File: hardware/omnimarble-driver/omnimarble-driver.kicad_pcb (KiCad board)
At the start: 4 copper layers, 220 x 150 mm, 178 parts, among them J1 BarrelJack_Horizontal, J10 PinSocket_1x20_P2.54mm_Vertic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, J11 PinHeader_2x13_P2.54mm_Vertic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, J2 TerminalBarrier_1x02_P9.50mm, J3 PinHeader_1x02_P2.54mm_Vertic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, J4 PinHeader_1x03_P2.54mm_Vertic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, J5 TerminalBarrier_1x02_P9.50mm, J6 IDC-Header_2x05_P2.54mm_Verti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, J7 IDC-Header_2x05_P2.54mm_Verti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, J8 JST_XH_B4B-XH-A_1x04_P2.50mm_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, J9 PinSocket_1x20_P2.54mm_Vertic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, K1 Relay_HF3FF_T73, K2 Relay_HF3FF_T73, Q1 SOT-23, Q10 TOLL-8, Q11 TOLL-8, Q12 TOLL-8, Q2 SOT-23, Q3 SOT-23, Q4 SOT-23, Q90 TO-252-2, Q91 TO-252-2, U1 TSOT-23-6, U10 VSSOP-8_2.3x2mm_P0.5mm, U11 SOIC-14_3.9x8.7mm_P1.27mm, U12 SOIC-14_3.9x8.7mm_P1.27mm, U2 SOT-89-3, U3 SOIC-8_3.9x4.9mm_P1.27mm, U4 SOIC-8_3.9x4.9mm_P1.27mm, U5 SOT-23, U6 SOT-353_SC-70-5, U7 SOIC-8_3.9x4.9mm_P1.27mm, U8 SOIC-8_3.9x4.9mm_P1.27mm, U9 TSSOP-8_3x3mm_P0.65mm

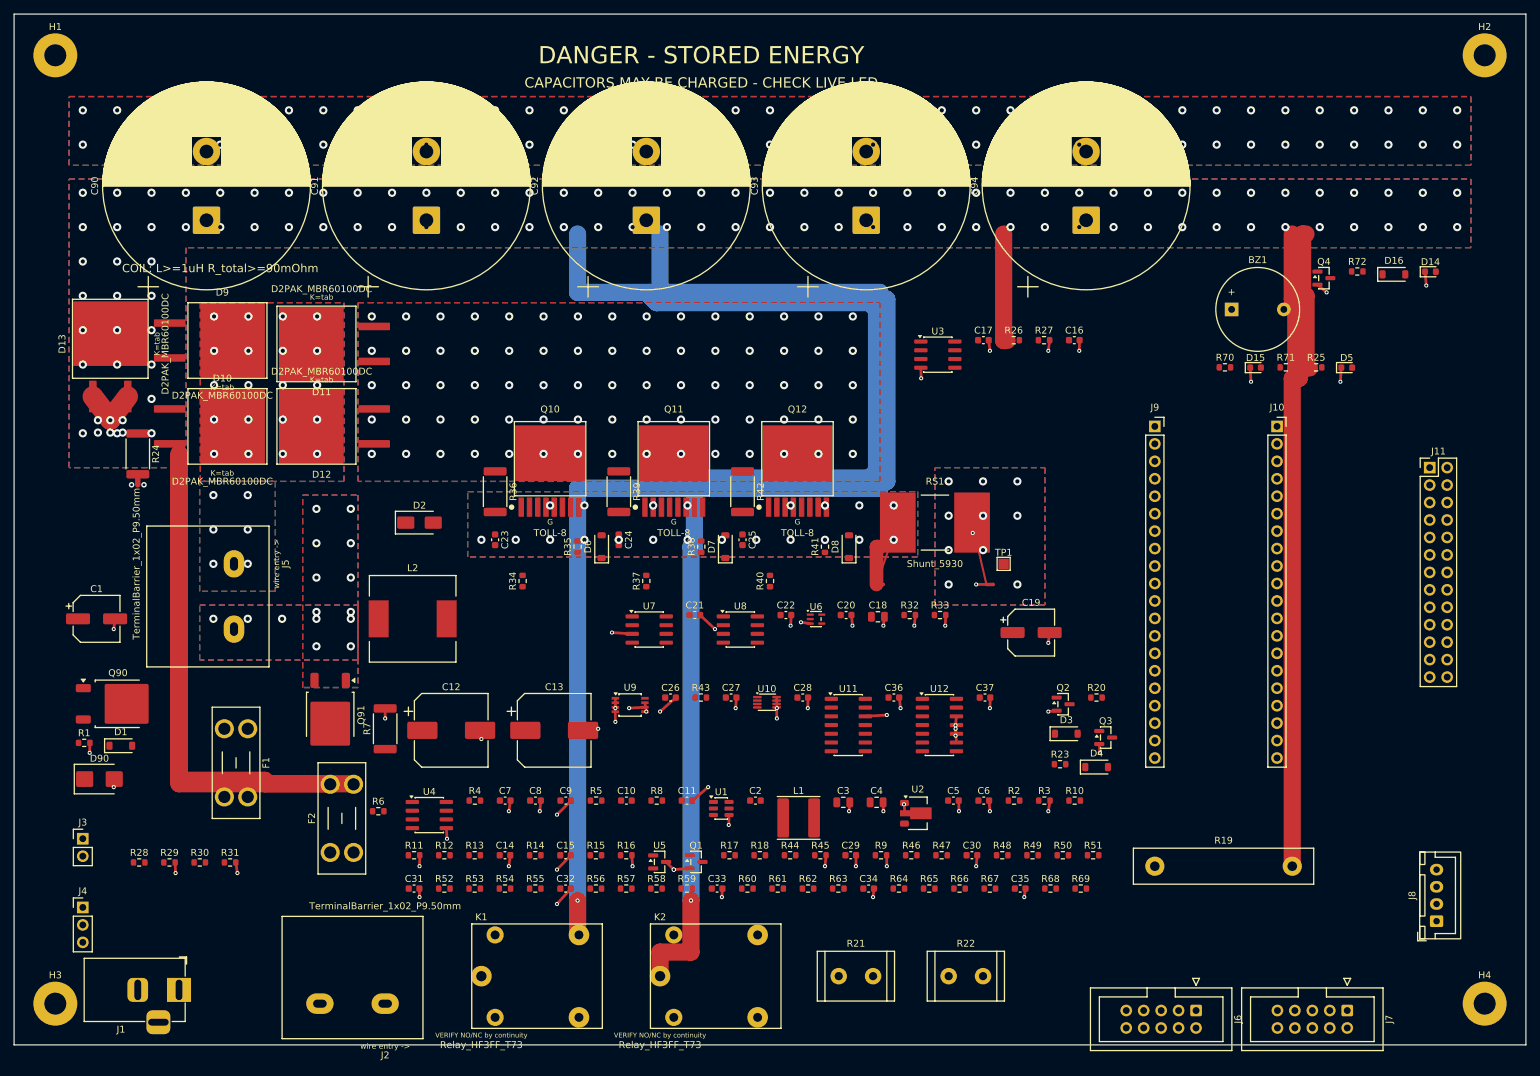
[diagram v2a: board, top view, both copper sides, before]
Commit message: Driver PCB: zero-shorts routing via parallel PathFinder negotiation
- gen_pcb.py: multiprocessing negotiation (24 workers, shared-memory
  usage/hist, sub-batch dispatch, ~14x wall time), best-state snapshot
  with restore-before-emit, stagnation break, width-aware swaths in all
  A* passes, verify-before-emit, contested-cell sentinel, tie/stub body
  checks, GND-drop relaxed site tests + far-ring recovery, straggler
  width ladder, geometric purge_track_shorts backstop
- route_worker.py: pcbnew-free worker module (Windows spawn safe)
- Board DRC: shorting_items 199 -> 0, tracks_crossing 25 -> 0,
  clearance 499 -> 56; unconnected 143 (honest residue: 52 route
  failures + GND drops + purged stubs) for the repair phase
- Reproducibility: deterministic across runs, worktree result
  reproduced exactly on main tree

Co-Authored-By: Claude Fable 5 <noreply@anthropic.com>
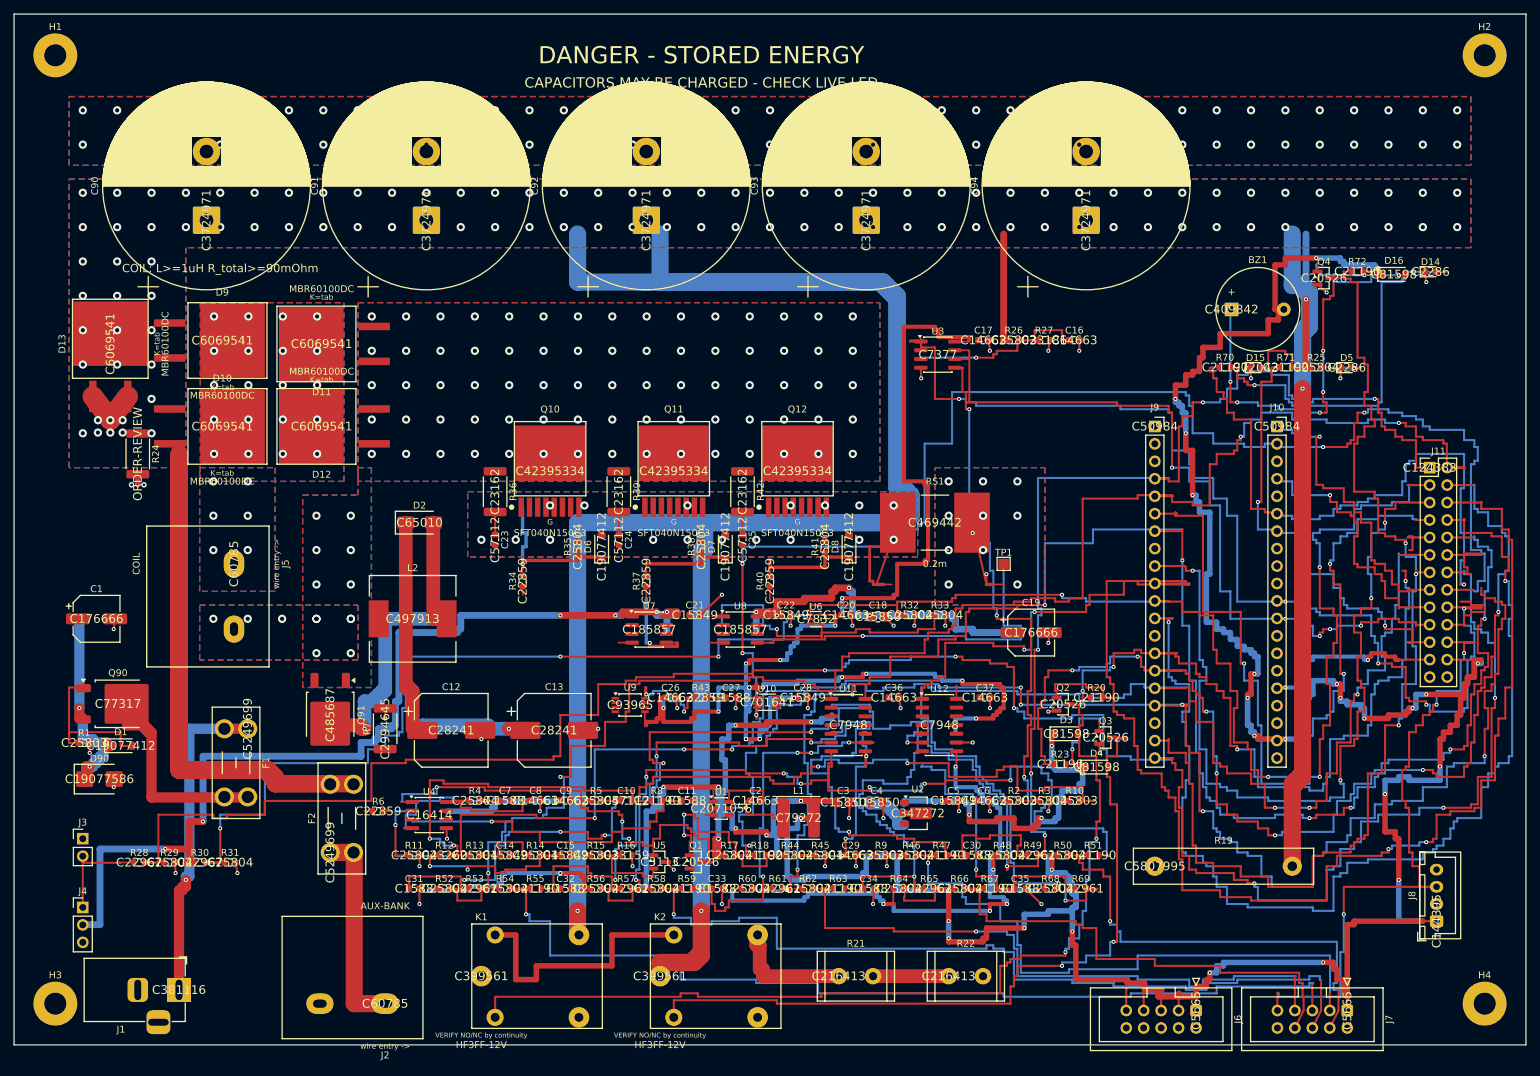
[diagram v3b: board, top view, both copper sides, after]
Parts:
- BZ1: value Buzzer_12x9.5RM7.6 -> buzzer-5V; footprint Buzzer_12x9.5RM7.6 -> Buzzer_Beeper:Buzzer_12x9.5RM7.6
- C1, C19: value CP_Elec_6.3x7.7 -> 100u-35V; footprint CP_Elec_6.3x7.7 -> Capacitor_SMD:CP_Elec_6.3x7.7
- C10, C23, C24, C25: value C_0603_1608Metric -> 10n; footprint C_0603_1608Metric -> Capacitor_SMD:C_0603_1608Metric
- C11, C27, C30, C31, C32, C33, C34, C35, C7: value C_0603_1608Metric -> 1n; footprint C_0603_1608Metric -> Capacitor_SMD:C_0603_1608Metric
- C12, C13: value CP_Elec_10x10.5 -> 100u-63V; footprint CP_Elec_10x10.5 -> Capacitor_SMD:CP_Elec_10x10.5
- C14, C15, C21, C22, C28, C5: value C_0603_1608Metric -> 1u; footprint C_0603_1608Metric -> Capacitor_SMD:C_0603_1608Metric
- C16, C17, C2, C20, C26, C29, C36, C37, C6, C8, C9: value C_0603_1608Metric -> 100n; footprint C_0603_1608Metric -> Capacitor_SMD:C_0603_1608Metric
- C18, C3, C4: value C_0805_2012Metric -> 10u; footprint C_0805_2012Metric -> Capacitor_SMD:C_0805_2012Metric
- C90, C91, C92, C93, C94: value CP_Radial_D30.0mm_P10.00mm_SnapIn -> 2200u-63V; footprint CP_Radial_D30.0mm_P10.00mm_SnapIn -> Capacitor_THT:CP_Radial_D30.0mm_P10.00mm_SnapIn
- D1, D6, D7, D8: value D_SOD-123 -> BZT52C15; footprint D_SOD-123 -> Diode_SMD:D_SOD-123
- D10, D11, D12, D13, D9: value D2PAK_MBR60100DC -> MBR60100DC; footprint D2PAK_MBR60100DC -> omnimarble:D2PAK_MBR60100DC
- D14, D5: value LED_0603_1608Metric -> LED_red; footprint LED_0603_1608Metric -> LED_SMD:LED_0603_1608Metric
- D15: value LED_0603_1608Metric -> LED_green; footprint LED_0603_1608Metric -> LED_SMD:LED_0603_1608Metric
- D16, D3, D4: value D_SOD-123 -> 1N4148W; footprint D_SOD-123 -> Diode_SMD:D_SOD-123
- D2: value D_SMA -> SS510; footprint D_SMA -> Diode_SMD:D_SMA
- D90: value D_SMB -> SMBJ33A; footprint D_SMB -> Diode_SMD:D_SMB
- F1: value Fuseholder_Blade_Mini_Keystone_3568 -> 5A-MINI; footprint Fuseholder_Blade_Mini_Keystone_3568 -> Fuse:Fuseholder_Blade_Mini_Keystone_3568
- F2: value Fuseholder_Blade_Mini_Keystone_3568 -> 30A-MINI; footprint Fuseholder_Blade_Mini_Keystone_3568 -> Fuse:Fuseholder_Blade_Mini_Keystone_3568
- J1: value BarrelJack_Horizontal -> 24V-IN; footprint BarrelJack_Horizontal -> Connector_BarrelJack:BarrelJack_Horizontal
- J10, J9: value PinSocket_1x20_P2.54mm_Vertical -> PICO-SOCKET; footprint PinSocket_1x20_P2.54mm_Vertical -> Connector_PinSocket_2.54mm:PinSocket_1x20_P2.54mm_Vertical
- J11: value PinHeader_2x13_P2.54mm_Vertical -> IO-BREAKOUT; footprint PinHeader_2x13_P2.54mm_Vertical -> Connector_PinHeader_2.54mm:PinHeader_2x13_P2.54mm_Vertical
- J2: value TerminalBarrier_1x02_P9.50mm -> AUX-BANK; footprint TerminalBarrier_1x02_P9.50mm -> omnimarble:TerminalBarrier_1x02_P9.50mm
- J3: value PinHeader_1x02_P2.54mm_Vertical -> E-STOP-NC; footprint PinHeader_1x02_P2.54mm_Vertical -> Connector_PinHeader_2.54mm:PinHeader_1x02_P2.54mm_Vertical
- J4: value PinHeader_1x03_P2.54mm_Vertical -> ARM-KEY; footprint PinHeader_1x03_P2.54mm_Vertical -> Connector_PinHeader_2.54mm:PinHeader_1x03_P2.54mm_Vertical
- J5: value TerminalBarrier_1x02_P9.50mm -> COIL; footprint TerminalBarrier_1x02_P9.50mm -> omnimarble:TerminalBarrier_1x02_P9.50mm
- J6: value IDC-Header_2x05_P2.54mm_Vertical -> RAIL-EMIT; footprint IDC-Header_2x05_P2.54mm_Vertical -> Connector_IDC:IDC-Header_2x05_P2.54mm_Vertical
- J7: value IDC-Header_2x05_P2.54mm_Vertical -> RAIL-RECV; footprint IDC-Header_2x05_P2.54mm_Vertical -> Connector_IDC:IDC-Header_2x05_P2.54mm_Vertical
- J8: value JST_XH_B4B-XH-A_1x04_P2.50mm_Vertical -> SPARE-JST; footprint JST_XH_B4B-XH-A_1x04_P2.50mm_Vertical -> Connector_JST:JST_XH_B4B-XH-A_1x04_P2.50mm_Vertical
- K1, K2: value Relay_HF3FF_T73 -> HF3FF-12V; footprint Relay_HF3FF_T73 -> omnimarble:Relay_HF3FF_T73
- L1: value L_Changjiang_FNR6045S -> 10uH; footprint L_Changjiang_FNR6045S -> Inductor_SMD:L_Changjiang_FNR6045S
- L2: value L_12x12mm_H8mm -> 47uH; footprint L_12x12mm_H8mm -> Inductor_SMD:L_12x12mm_H8mm
- NT1, NT2: value NetTie-2_SMD_Pad0.5mm -> NetTie; footprint NetTie-2_SMD_Pad0.5mm -> NetTie:NetTie-2_SMD_Pad0.5mm
- Q1, Q2, Q3, Q4: value SOT-23 -> MMBT3904; footprint SOT-23 -> Package_TO_SOT_SMD:SOT-23
- Q10, Q11, Q12: value TOLL-8 -> SFT040N150C3; footprint TOLL-8 -> omnimarble:TOLL-8
- Q90: value TO-252-2 -> AOD4185; footprint TO-252-2 -> Package_TO_SOT_SMD:TO-252-2
- Q91: value TO-252-2 -> AOD66923; footprint TO-252-2 -> Package_TO_SOT_SMD:TO-252-2
- R1, R10, R15, R2, R26, R9: value R_0603_1608Metric -> 100k; footprint R_0603_1608Metric -> Resistor_SMD:R_0603_1608Metric
- R11, R13, R14, R17, R25, R29, R3, R31, R32, R33, R35, R38, R4, R41, R44, R45, R46, R48, R5, R50, R52, R54, R56, R58, R60, R62, R64, R66, R68: value R_0603_1608Metric -> 10k; footprint R_0603_1608Metric -> Resistor_SMD:R_0603_1608Metric
- R12: value R_0603_1608Metric -> 9.1k; footprint R_0603_1608Metric -> Resistor_SMD:R_0603_1608Metric
- R16: value R_0603_1608Metric -> 4.3k; footprint R_0603_1608Metric -> Resistor_SMD:R_0603_1608Metric
- R18, R20, R23, R47, R51, R55, R59, R63, R67, R70, R71, R72, R8: value R_0603_1608Metric -> 1k; footprint R_0603_1608Metric -> Resistor_SMD:R_0603_1608Metric
- R19: value R_Box_L26.0mm_W5.0mm_P20.00mm -> 47R-5W; footprint R_Box_L26.0mm_W5.0mm_P20.00mm -> Resistor_THT:R_Box_L26.0mm_W5.0mm_P20.00mm
- R21, R22: value R_Radial_Power_L11.0mm_W7.0mm_P5.00mm -> 100R-10W; footprint R_Radial_Power_L11.0mm_W7.0mm_P5.00mm -> Resistor_THT:R_Radial_Power_L11.0mm_W7.0mm_P5.00mm
- R24: value R_2512_6332Metric -> 6.8k-2W; footprint R_2512_6332Metric -> Resistor_SMD:R_2512_6332Metric
- R27: value R_0603_1608Metric -> 5.1k; footprint R_0603_1608Metric -> Resistor_SMD:R_0603_1608Metric
- R28, R30: value R_0603_1608Metric -> 27k; footprint R_0603_1608Metric -> Resistor_SMD:R_0603_1608Metric
- R34, R37, R40, R43, R6: value R_0603_1608Metric -> 10R; footprint R_0603_1608Metric -> Resistor_SMD:R_0603_1608Metric
- R36, R39, R42: value R_2512_6332Metric -> 4.7k; footprint R_2512_6332Metric -> Resistor_SMD:R_2512_6332Metric
- R49, R53, R57, R61, R65, R69: value R_0603_1608Metric -> 220k; footprint R_0603_1608Metric -> Resistor_SMD:R_0603_1608Metric
- R7: value R_2512_6332Metric -> 0.05R-2512; footprint R_2512_6332Metric -> Resistor_SMD:R_2512_6332Metric
- RS1: value Shunt_5930 -> 0.2m; footprint Shunt_5930 -> omnimarble:Shunt_5930
- TP1: value TestPoint_Pad_1.5x1.5mm -> DRV_SPARE; footprint TestPoint_Pad_1.5x1.5mm -> TestPoint:TestPoint_Pad_1.5x1.5mm
- U1: value TSOT-23-6 -> AP63205; footprint TSOT-23-6 -> Package_TO_SOT_SMD:TSOT-23-6
- U10: value VSSOP-8_2.3x2mm_P0.5mm -> ADS7042; footprint VSSOP-8_2.3x2mm_P0.5mm -> Package_SO:VSSOP-8_2.3x2mm_P0.5mm
- U11, U12: value SOIC-14_3.9x8.7mm_P1.27mm -> LM339; footprint SOIC-14_3.9x8.7mm_P1.27mm -> Package_SO:SOIC-14_3.9x8.7mm_P1.27mm
- U2: value SOT-89-3 -> 78L12; footprint SOT-89-3 -> Package_TO_SOT_SMD:SOT-89-3
- U3: value SOIC-8_3.9x4.9mm_P1.27mm -> MCP6002; footprint SOIC-8_3.9x4.9mm_P1.27mm -> Package_SO:SOIC-8_3.9x4.9mm_P1.27mm
- U4: value SOIC-8_3.9x4.9mm_P1.27mm -> UC3843B; footprint SOIC-8_3.9x4.9mm_P1.27mm -> Package_SO:SOIC-8_3.9x4.9mm_P1.27mm
- U5: value SOT-23 -> CJ431-0.5%; footprint SOT-23 -> Package_TO_SOT_SMD:SOT-23
- U6: value SOT-353_SC-70-5 -> 74LVC1G08; footprint SOT-353_SC-70-5 -> Package_TO_SOT_SMD:SOT-353_SC-70-5
- U7, U8: value SOIC-8_3.9x4.9mm_P1.27mm -> UCC27524A; footprint SOIC-8_3.9x4.9mm_P1.27mm -> Package_SO:SOIC-8_3.9x4.9mm_P1.27mm
- U9: value TSSOP-8_3x3mm_P0.65mm -> INA240A1; footprint TSSOP-8_3x3mm_P0.65mm -> Package_SO:TSSOP-8_3x3mm_P0.65mm
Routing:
- net +5V: track 0.00 -> 590.7 mm, vias 0 -> 40
- net 3V3: track 0.00 -> 390.9 mm, vias 0 -> 28
- net ESTOP_SENSE: track 0.00 -> 326.8 mm, vias 0 -> 6
- net GATE6: track 0.00 -> 309.1 mm, vias 0 -> 6
- net ARM_SENSE: track 0.00 -> 297.1 mm, vias 0 -> 5
- net VSET_PWM: track 0.00 -> 275.8 mm, vias 0 -> 8
- net GATE4: track 0.00 -> 274.9 mm, vias 0 -> 9
- net GATE2: track 0.00 -> 247.3 mm, vias 0 -> 4
- net GATE1: track 0.00 -> 212.9 mm, vias 0 -> 6
- net ADC_CS: track 0.00 -> 208.3 mm, vias 0 -> 6
- net +12V_SW: track 0.00 -> 207.5 mm, vias 0 -> 10
- net GATE3: track 0.00 -> 207.3 mm, vias 0 -> 6
- net BOOST_EN_N: track 0.00 -> 198.6 mm, vias 0 -> 4
- net BUZZ: track 0.00 -> 171.5 mm, vias 0 -> 3
- net MCU_FIRE: track 0.00 -> 171.3 mm, vias 0 -> 4
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
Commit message: Driver PCB: repair pass + KiCad-10 via-assert fix (unconnected 143->118)
- Fix repair/grid-build hang: PCB_VIA.GetWidth() with no layer arg fires
  a blocking wx assert in KiCad 10 (only triggered when loading an
  already-routed board with vias, so scripted mode never hit it). Read
  diameter with a layer arg, fall back to 0.6mm.
- main_repair now runs purge_track_shorts before save, so closing
  unconnected pairs can never leave a short behind.
- Board: shorts 0, crossings 0, clearance 58, unconnected 143->118
  (repair routed 82, purge removed 9 boundary touches). Residual
  unconnected are long cross-board signal nets for manual finishing.

Co-Authored-By: Claude Fable 5 <noreply@anthropic.com>
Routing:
- net +12V: track 111.6 -> 585.3 mm, vias 7 -> 26
- net 3V3: track 390.9 -> 544.1 mm, vias 28 -> 42
- net ARM_SENSE: track 297.1 -> 359.1 mm, vias 5 -> 6
- net +5V: track 590.7 -> 643.4 mm, vias 40 -> 45
- net FIRE_GATED: track 49.2 -> 97.8 mm, vias 1 -> 5
- net VTH_GATE: track 44.8 -> 59.3 mm, vias 4 -> 5
- net GATE4: track 274.9 -> 284.4 mm, vias 9 -> 10
- net +12V_SW: track 207.5 -> 216.9 mm, vias 10 -> 12
- net BST_SW: track 49.8 -> 58.8 mm, vias 1 -> 2
- net RLY_CHARGE: track 119.3 -> 127.3 mm
- net LED_ARMED: track 104.8 -> 111.8 mm, vias 2 -> 3
- net SIG5: track 93.6 -> 98.8 mm
- net BOOST_EN_N: track 198.6 -> 203.5 mm
- net SIG4: track 125.2 -> 130.1 mm
- net RLY_DUMP: track 167.6 -> 172.0 mm
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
